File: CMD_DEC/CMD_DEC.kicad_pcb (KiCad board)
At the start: 2 copper layers, 73.7 x 48.3 mm, 22 parts, among them J1 Conn_01x04_Male, J10 Conn_01x01_Male, J11 Conn_01x01_Male, J12 Conn_01x01_Male, J2 Conn_01x02_Male, J3 Conn_01x05_Male, J4 Conn_01x08_Male, J5 Conn_01x08_Male, J6 Conn_01x02_Male, J7 Conn_01x01_Male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

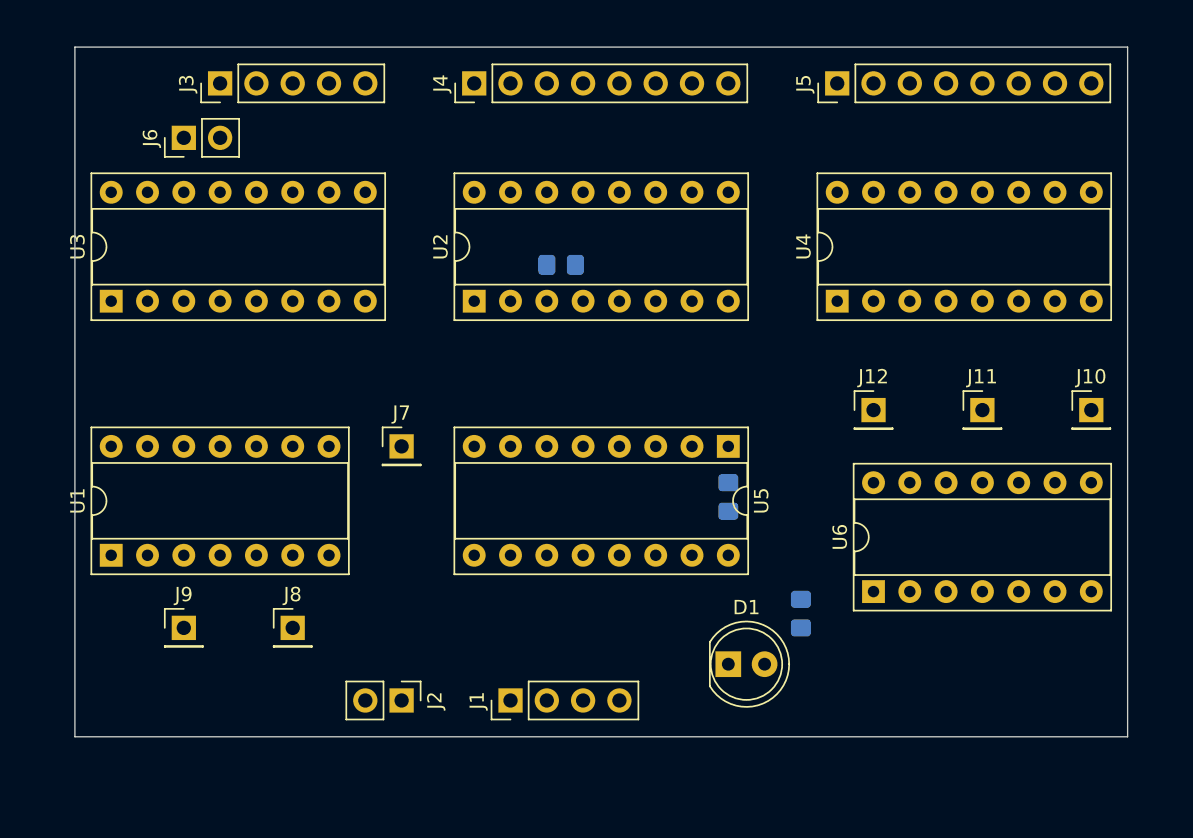
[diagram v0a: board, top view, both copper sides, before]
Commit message: Command decoder in work
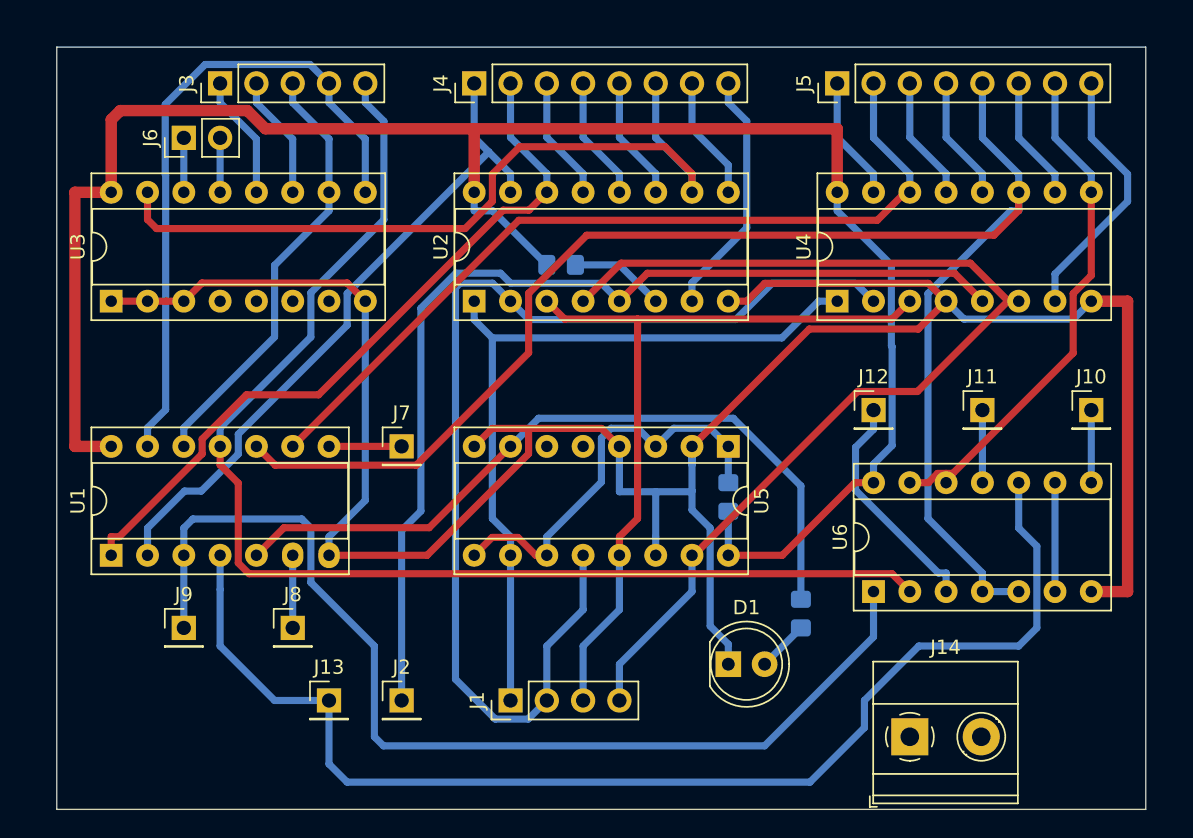
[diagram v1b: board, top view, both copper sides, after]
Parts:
- added J13: Conn_01x01_Male, Connector_PinHeader_2.54mm:PinHeader_1x01_P2.54mm_Vertical, F.Cu at (48.3, 76.2)
- added J14: Screw_Terminal_01x02, TerminalBlock_Phoenix:TerminalBlock_Phoenix_MKDS-1,5-2_1x02_P5.00mm_Horizontal, F.Cu at (88.9, 78.7)
- J2: value Conn_01x02_Male -> Conn_01x01_Male; footprint Connector_PinHeader_2.54mm:PinHeader_1x02_P2.54mm_Vertical -> Connector_PinHeader_2.54mm:PinHeader_1x01_P2.54mm_Vertical
- turned J2 to 0 degrees
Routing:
- net GND: track 0.00 -> 172.7 mm
- net VCC: track 0.00 -> 134.2 mm
- net /~ST: track 0.00 -> 108.7 mm
- net /~LSRx: track 0.00 -> 87.2 mm
- net /C2: track 0.00 -> 86.3 mm
- net /COP[1]: track 0.00 -> 78.7 mm
- net /COP[3]: track 0.00 -> 74.4 mm
- net /~ADDx: track 0.00 -> 74.4 mm
- net /C1: track 0.00 -> 70.7 mm
- net /~LD: track 0.00 -> 59.2 mm
- net /COP[2]: track 0.00 -> 54.7 mm
- net /~UNO: track 0.00 -> 54.5 mm
- net /COP[0]: track 0.00 -> 54.2 mm
- net /WILL_WR2REG: track 0.00 -> 52.0 mm
- net /~ADDC: track 0.00 -> 51.0 mm
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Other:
- board size 73.7 x 48.3 mm -> 76.2 x 53.3 mm

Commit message: Cmd dec in work
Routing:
- net VCC: track 134.2 -> 226.3 mm
- net GND: track 172.7 -> 189.1 mm
- net /C2: track 86.3 -> 84.2 mm
- net /~CMP: track 36.3 -> 37.9 mm
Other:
- board size 76.2 x 53.3 mm -> 76.2 x 54.6 mm

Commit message: Cmd dec in work
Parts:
- moved J1 33.4 mm to (94.0, 71.1), turned to 270 degrees
- moved J11 30.2 mm to (67.9, 71.1)
- moved U6 28.1 mm to (58.4, 66.0)
- moved J10 28.0 mm to (73.7, 54.6)
- moved J12 27.5 mm to (63.5, 71.1)
- moved J2 26.5 mm to (43.8, 51.4)
- moved R1 25.4 mm to (39.1, 44.5)
- moved J3 25.4 mm to (66.0, 33.0)
- moved J4 25.4 mm to (33.0, 33.0)
- moved J6 25.4 mm to (63.5, 36.8)
- moved U2 25.4 mm to (33.0, 48.3)
- moved U3 25.4 mm to (58.4, 48.3)
- moved D1 25.4 mm to (101.6, 73.7), turned to 180 degrees
- moved R5 17.8 mm to (99.1, 70.2)
- moved J14 15.2 mm to (73.7, 78.7)
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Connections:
- U1 pad 1: /~ADDC -> /WILL_WR2REG
- U1 pad 12: /~LSR -> /~LSRC
- U1 pad 13: /~LSRC -> /~LSR
- U1 pad 2: /~ADD -> /C2
- U1 pad 3: /~ADDx -> /LATCH_REG
- U1 pad 4: /C2 -> /~ADD
- U1 pad 5: /WILL_WR2REG -> /~ADDC
- U1 pad 6: /LATCH_REG -> /~ADDx
- U6 pad 11: /CMP_EN -> Net-(U6-Pad11)
- U6 pad 12: /~CMP -> /~ST
- U6 pad 13: /~CMP -> /~ST
- U6 pad 4: /~ST -> /~CMP
- U6 pad 5: /~ST -> /~CMP
- U6 pad 6: Net-(U6-Pad6) -> /CMP_EN
- U6 pad 9: Net-(U6-Pad6) -> Net-(U6-Pad11)
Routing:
- net /COP[2]: track 54.7 -> 128.6 mm
- net /COP[0]: track 54.2 -> 114.0 mm
- net /~ADDx: track 74.4 -> 18.4 mm
- net /COP[3]: track 74.4 -> 120.5 mm
- net /WILL_WR2REG: track 52.0 -> 88.4 mm
- net /~UNO: track 54.5 -> 24.4 mm
- net /~ST: track 108.7 -> 79.7 mm
- net /~LSR: track 30.7 -> 58.6 mm
- net /C2: track 84.2 -> 58.2 mm
- net /~CMP: track 37.9 -> 58.8 mm
- net VCC: track 226.3 -> 246.7 mm
- net GND: track 189.1 -> 205.5 mm
- net /~LSRx: track 87.2 -> 71.1 mm
- net /~LD: track 59.2 -> 73.2 mm
- net /COP[1]: track 78.7 -> 91.5 mm, vias 0 -> 1
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
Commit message: Polishing Cmd dec
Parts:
- added H1: MountingHole, MountingHole:MountingHole_3.2mm_M3, F.Cu at (58.4, 33.0)
- added H2: MountingHole, MountingHole:MountingHole_3.2mm_M3, F.Cu at (102.9, 76.2)
- added H3: MountingHole, MountingHole:MountingHole_3.2mm_M3, F.Cu at (31.8, 76.2)
- moved J9 41.0 mm to (30.5, 33.0)
- moved D1 20.5 mm to (104.1, 53.3)
- moved R5 9.42 mm to (103.6, 62.0), turned to 90 degrees
- moved J13 5.68 mm to (50.8, 71.1)
- moved J10 4.26 mm to (77.5, 56.5)
- moved J14 4.02 mm to (74.9, 74.9)
- moved J8 3.81 mm to (43.2, 71.1)
- moved R2 1.91 mm to (82.5, 62.2)
- moved J2 0.28 mm to (43.7, 51.7)
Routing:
- net /~ADDx: track 18.4 -> 71.1 mm
- net Net-(D1-Pad2): track 2.44 -> 8.48 mm
- net VCC: track 246.7 -> 240.8 mm
- net /~CMP: track 58.8 -> 64.1 mm
- net /C2: track 58.2 -> 53.5 mm
- net /LATCH_REG: track 6.35 -> 9.04 mm
- net /COP[1]: track 91.5 -> 93.9 mm
- net /~RAM_WR: track 3.81 -> 5.72 mm
- net Net-(R2-Pad1): track 36.5 -> 38.0 mm
- net /COP[3]: track 120.5 -> 119.1 mm
- net /~ST: track 79.7 -> 80.8 mm
- net GND: track 205.5 -> 206.4 mm
- net /WILL_WR2REG: track 88.4 -> 89.3 mm
- net /C1: track 63.1 -> 63.9 mm
- net /COP[2]: track 128.6 -> 128.0 mm
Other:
- board size 76.2 x 54.6 mm -> 78.7 x 50.8 mm
- board text added: "C1"
- board text added: "C2"
- board text added: "CF_EN"
- board text added: "CMP_EN"
- board text added: "COP[3:0]"
- board text added: "Gnd"
- board text added: "LATCH REG"
- board text added: "SRC[0:1]"
- board text added: "Vcc"
- board text added: "~ADD"
- board text added: "~ADDC"
- board text added: "~ADDx"
- board text added: "~AND"
- board text added: "~BR"
- board text added: "~CMP"
- board text added: "~CTRL"
- board text added: "~IN"
- board text added: "~INV"
- board text added: "~LD"
- board text added: "~LDI"
- board text added: "~LSR"
- board text added: "~LSRC"
- board text added: "~LSRx"
- board text added: "~MOV"
- board text added: "~MUL"
- board text added: "~OR"
- board text added: "~OUT"
- board text added: "~RAM_CS"
- board text added: "~RAM_WR"
- board text added: "~ST"
- board text added: "~SWAP"
- board text added: "~UNO"
- board text added: "~XOR"

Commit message: Polishing Cmd dec
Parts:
- added C1: 0.1uF, Capacitor_SMD:C_0805_2012Metric_Pad1.18x1.45mm_HandSolder, F.Cu at (46.5, 62.2)
- added C3: 0.1uF, Capacitor_SMD:C_0805_2012Metric_Pad1.18x1.45mm_HandSolder, F.Cu at (61.0, 43.8)
- added C4: 0.1uF, Capacitor_SMD:C_0805_2012Metric_Pad1.18x1.45mm_HandSolder, F.Cu at (86.2, 43.5)
- added C5: 0.1uF, Capacitor_SMD:C_0805_2012Metric_Pad1.18x1.45mm_HandSolder, F.Cu at (86.2, 62.2)
- added C6: 0.1uF, Capacitor_SMD:C_0805_2012Metric_Pad1.18x1.45mm_HandSolder, F.Cu at (61.1, 62.2)
- added J15: Conn_01x03_Male, Connector_PinHeader_2.54mm:PinHeader_1x03_P2.54mm_Vertical, F.Cu at (62.9, 52.7)
- added J16: Conn_01x04_Male, Connector_PinHeader_2.54mm:PinHeader_1x04_P2.54mm_Vertical, F.Cu at (67.0, 52.7)
- added J17: Conn_01x01_Male, Connector_PinHeader_2.54mm:PinHeader_1x01_P2.54mm_Vertical, F.Cu at (36.2, 52.7)
- moved J10 1.91 mm to (77.5, 58.4)
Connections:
- U3 pad 1: GND -> Net-(J15-Pad3)
- U3 pad 2: GND -> Net-(J15-Pad2)
- U3 pad 3: GND -> Net-(J15-Pad1)
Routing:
- net VCC: track 240.8 -> 252.0 mm
- net /~LD: track 73.2 -> 81.6 mm
- net Net-(J16-Pad4): track 0.00 -> 4.84 mm
- net Net-(J16-Pad3): track 0.00 -> 4.84 mm
- net Net-(J16-Pad2): track 0.00 -> 4.84 mm
- net Net-(J16-Pad1): track 0.00 -> 4.84 mm
- net Net-(J15-Pad3): track 0.00 -> 4.71 mm
- net Net-(J15-Pad2): track 0.00 -> 4.71 mm
- net Net-(J15-Pad1): track 0.00 -> 4.71 mm
- net GND: track 206.4 -> 201.7 mm
- net /~RAM_WR: track 5.72 -> 3.81 mm
- net /~CMP: track 64.1 -> 65.5 mm
- net /~ST: track 80.8 -> 81.9 mm
- net /COP[3]: track 119.1 -> 120.2 mm
- net /~LSRx: track 71.1 -> 71.8 mm
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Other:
- net class Default: trace_width 0.5 -> 0.4
- rule trace_min: 0.5 -> 0.4
- board text added: "0"
- board text added: "1"
- board text added: "2"
- board text added: "3"
- board text added: "A0"
- board text added: "A1"
- board text added: "E"
- board text added: "~RAM_OE"

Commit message: Polishing CMD DEC
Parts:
- added J18: Conn_01x01_Male, Connector_PinHeader_2.54mm:PinHeader_1x01_P2.54mm_Vertical, F.Cu at (99.1, 71.1)
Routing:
- net GND: track 201.7 -> 202.6 mm
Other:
- board text added: "23.05.2023"
- board text added: "74HCPU"
- board text added: "CMD DEC"
- board text added: "ZF_EN"

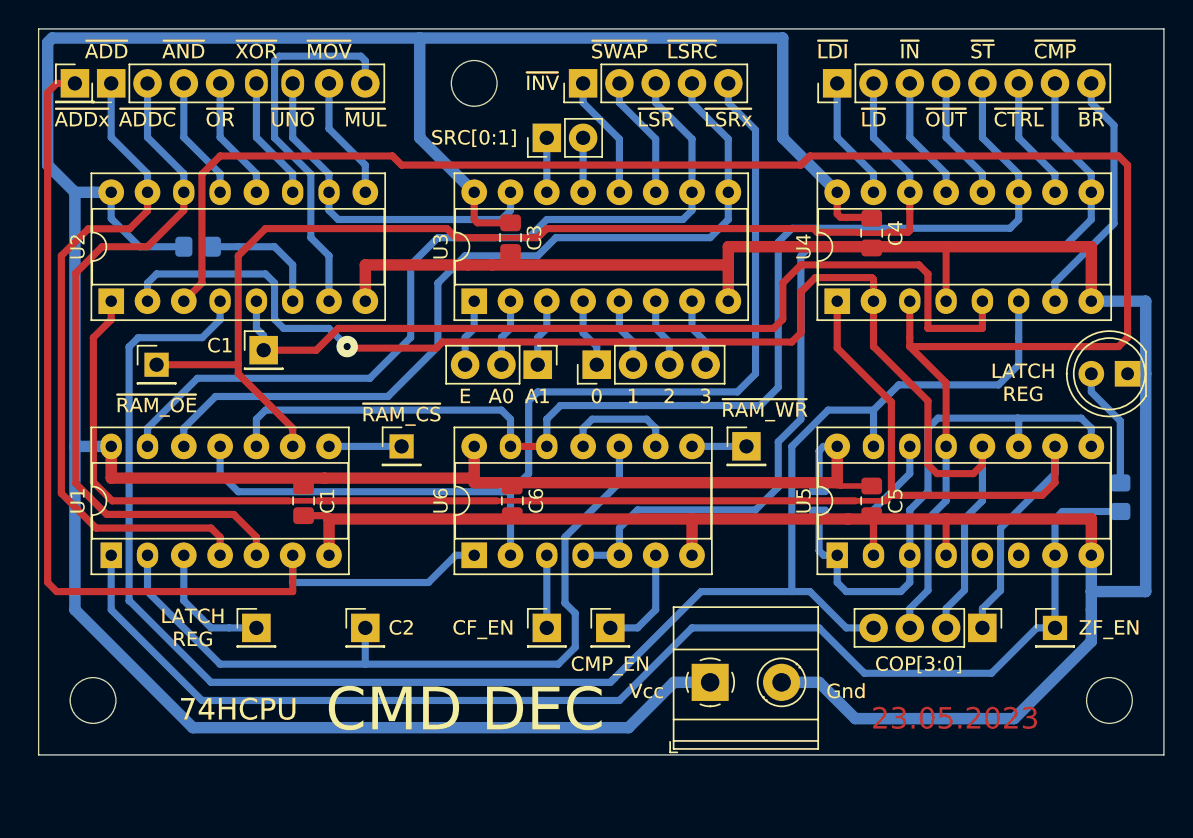
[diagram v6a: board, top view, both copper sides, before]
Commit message: Add additional pin MUL
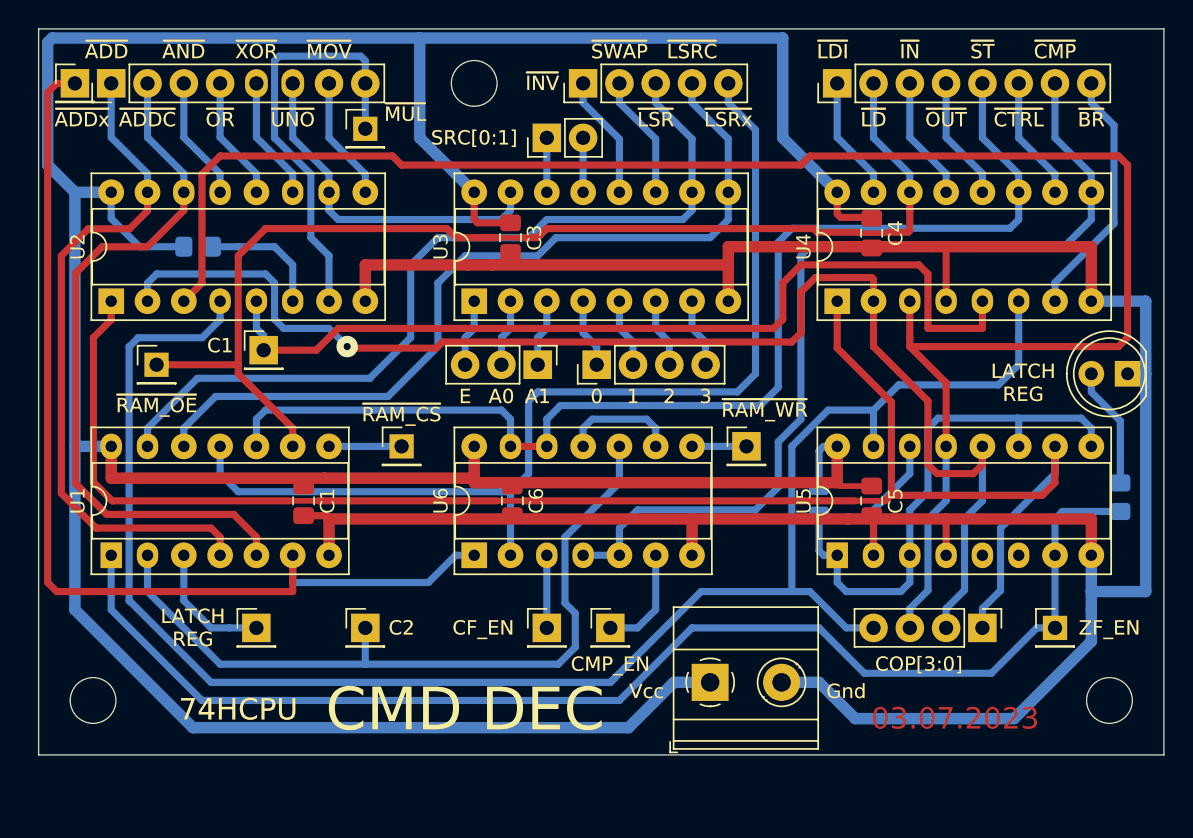
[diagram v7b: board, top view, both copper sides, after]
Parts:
- added J19: Conn_01x01_Male, Connector_PinHeader_2.54mm:PinHeader_1x01_P2.54mm_Vertical, F.Cu at (50.8, 36.2)
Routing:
- net /~MUL: track 26.6 -> 29.8 mm
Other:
- board text added: "03.07.2023"
- board text removed: "23.05.2023"
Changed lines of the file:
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@@
     (thickness 1.6)
     (drawings 94)
-    (tracks 464)
+    (tracks 465)
     (zones 0)
-    (modules 36)
+    (modules 37)
     (nets 52)
   )
@@
   )
   (module Connector_PinHeader_2.54mm:PinHeader_1x01_P2.54mm_Vertical (layer F.Cu)
+    (at 50.8 36.195)
+    (descr "Through hole straight pin header, 1x01, 2.54mm pitch, single row")
+    (tags "Through hole pin header THT 1x01 2.54mm single row")
+    (fp_text reference J19 (at 2.54 -0.3175) (layer F.SilkS) hide
+      (effects (font (size 1 1) (thickness 0.15)))
+    )
+    (fp_text value Conn_01x01_Male (at 0 2.33) (layer F.Fab)
+      (effects (font (size 1 1) (thickness 0.15)))
+    )
+    (fp_line (start 1.8 -1.8) (end -1.8 -1.8) (layer F.CrtYd) (width 0.05))
+    (fp_line (start 1.8 1.8) (end 1.8 -1.8) (layer F.CrtYd) (width 0.05))
+    (fp_line (start -1.8 1.8) (end 1.8 1.8) (layer F.CrtYd) (width 0.05))
+    (fp_line (start -1.8 -1.8) (end -1.8 1.8) (layer F.CrtYd) (width 0.05))
+    (fp_line (start -1.33 -1.33) (end 0 -1.33) (layer F.SilkS) (width 0.12))
+    (fp_line (start -1.33 0) (end -1.33 -1.33) (layer F.SilkS) (width 0.12))
+    (fp_line (start -1.33 1.27) (end 1.33 1.27) (layer F.SilkS) (width 0.12))
+    (fp_line (start 1.33 1.27) (end 1.33 1.33) (layer F.SilkS) (width 0.12))
+    (fp_line (start -1.33 1.27) (end -1.33 1.33) (layer F.SilkS) (width 0.12))
+    (fp_line (start -1.33 1.33) (end 1.33 1.33) (layer F.SilkS) (width 0.12))
+    (fp_line (start -1.27 -0.635) (end -0.635 -1.27) (layer F.Fab) (width 0.1))
+    (fp_line (start -1.27 1.27) (end -1.27 -0.635) (layer F.Fab) (width 0.1))
+    (fp_line (start 1.27 1.27) (end -1.27 1.27) (layer F.Fab) (width 0.1))
+    (fp_line (start 1.27 -1.27) (end 1.27 1.27) (layer F.Fab) (width 0.1))
+    (fp_line (start -0.635 -1.27) (end 1.27 -1.27) (layer F.Fab) (width 0.1))
+    (fp_text user %R (at 0 0 90) (layer F.Fab)
+      (effects (font (size 1 1) (thickness 0.15)))
+    )
+    (pad 1 thru_hole rect (at 0 0) (size 1.7 1.7) (drill 1) (layers *.Cu *.Mask)
+      (net 21 /~MUL))
+    (model ${KISYS3DMOD}/Connector_PinHeader_2.54mm.3dshapes/PinHeader_1x01_P2.54mm_Vertical.wrl
+      (at (xyz 0 0 0))
+      (scale (xyz 1 1 1))
+      (rotate (xyz 0 0 0))
+    )
+  )
+  (module Connector_PinHeader_2.54mm:PinHeader_1x01_P2.54mm_Vertical (layer F.Cu)
     (at 99.06 71.12)
     (descr "Through hole straight pin header, 1x01, 2.54mm pitch, single row")
@@
     (effects (font (size 1.5 1.5) (thickness 0.3)))
   )
-  (gr_text 23.05.2023 (at 92.075 77.47) (layer F.Cu)
+  (gr_text 03.07.2023 (at 92.075 77.47) (layer F.Cu)
     (effects (font (size 1.5 1.5) (thickness 0.3)))
   )
@@
     (effects (font (size 1 1) (thickness 0.15)))
   )
-  (gr_text ~MUL (at 50.8 35.56) (layer F.Cu)
+  (gr_text ~MUL (at 53.594 35.179) (layer F.Cu)
     (effects (font (size 1 1) (thickness 0.15)))
   )
@@
     (effects (font (size 1 1) (thickness 0.15)))
   )
-  (gr_text ~MUL (at 50.8 35.56) (layer F.SilkS)
+  (gr_text ~MUL (at 53.594 35.179) (layer F.SilkS)
     (effects (font (size 1 1) (thickness 0.15)))
   )
@@
   (segment (start 60.96 41.91) (end 60.96 40.64) (width 0.5) (layer B.Cu) (net 19))
   (segment (start 60.325 42.545) (end 60.96 41.91) (width 0.5) (layer B.Cu) (net 19))
-  (segment (start 48.26 33.02) (end 48.26 36.195) (width 0.5) (layer B.Cu) (net 20))
-  (segment (start 48.26 36.195) (end 50.8 38.735) (width 0.5) (layer B.Cu) (net 20))
-  (segment (start 50.8 38.735) (end 50.8 40.64) (width 0.5) (layer B.Cu) (net 20))
+  (segment (start 50.8 39.37) (end 50.8 40.64) (width 0.5) (layer B.Cu) (net 20))
+  (segment (start 48.26 36.83) (end 50.8 39.37) (width 0.5) (layer B.Cu) (net 20))
+  (segment (start 48.26 33.02) (end 48.26 36.83) (width 0.5) (layer B.Cu) (net 20))
   (segment (start 50.8 31.4325) (end 50.8 33.02) (width 0.5) (layer B.Cu) (net 21))
   (segment (start 50.4825 31.115) (end 50.8 31.4325) (width 0.5) (layer B.Cu) (net 21))
@@
   (segment (start 48.26 45.085) (end 46.99 43.815) (width 0.5) (layer B.Cu) (net 21))
   (segment (start 48.26 48.26) (end 48.26 45.085) (width 0.5) (layer B.Cu) (net 21))
+  (segment (start 50.8 33.02) (end 50.8 36.195) (width 0.5) (layer B.Cu) (net 21))
   (segment (start 103.1875 42.8325) (end 99.06 46.96) (width 0.5) (layer B.Cu) (net 22))
   (segment (start 99.06 46.96) (end 99.06 48.26) (width 0.5) (layer B.Cu) (net 22))

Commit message: Polishing CMD DEC
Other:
- board text added: "00"
- board text added: "08"
- board text added: "138"
- board text added: "139"
- board text added: "85"
